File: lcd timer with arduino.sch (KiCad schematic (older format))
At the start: 30 parts, among them J1 Conn_01x05_Female, J2 Screw_Terminal_01x02, J3 Screw_Terminal_01x02, J4 Screw_Terminal_01x02, K1 SANYOU_SRD_Form_C, K2 SANYOU_SRD_Form_C, K3 SANYOU_SRD_Form_C, K4 SANYOU_SRD_Form_C, Q1 2N3904, Q2 2N3904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

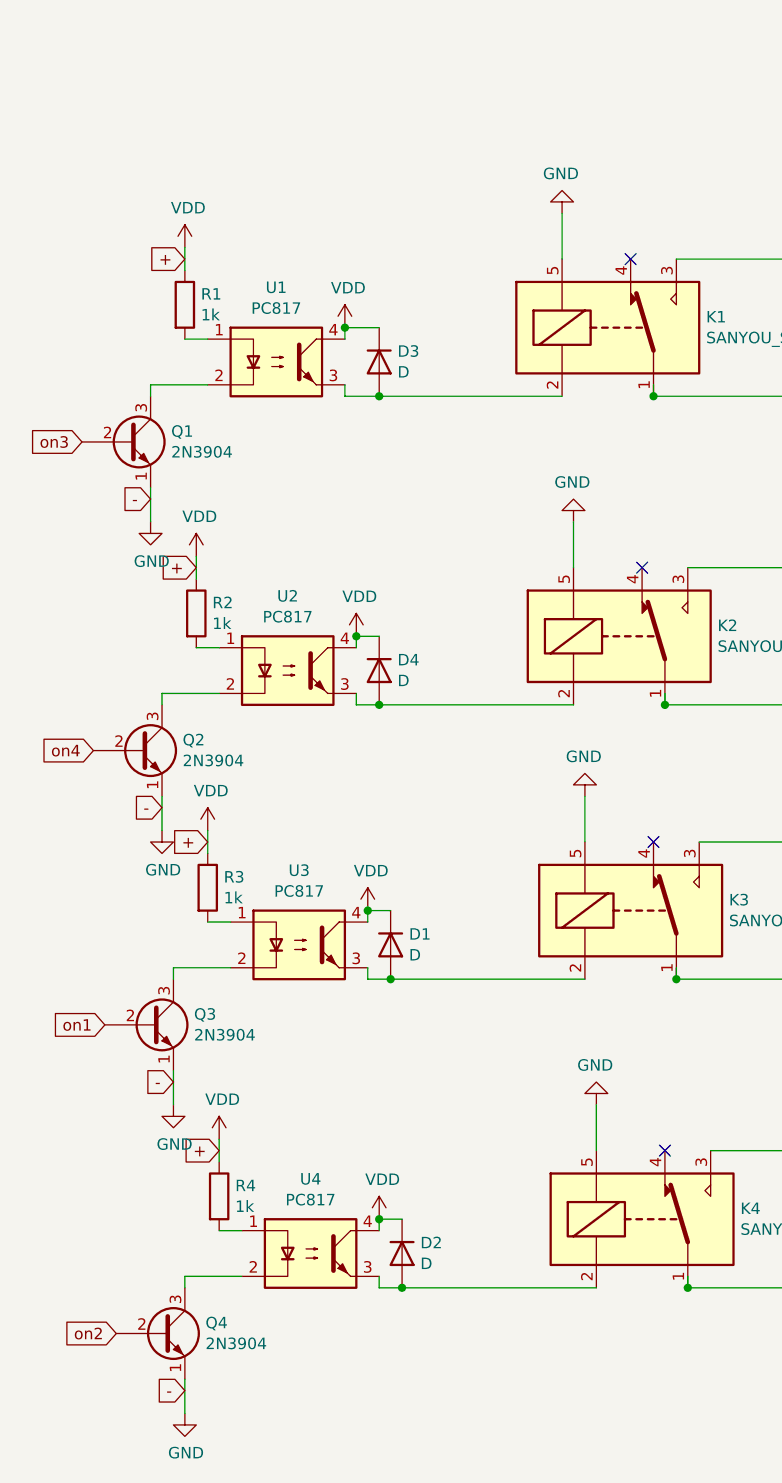
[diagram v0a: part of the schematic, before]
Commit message: fixed the schematic
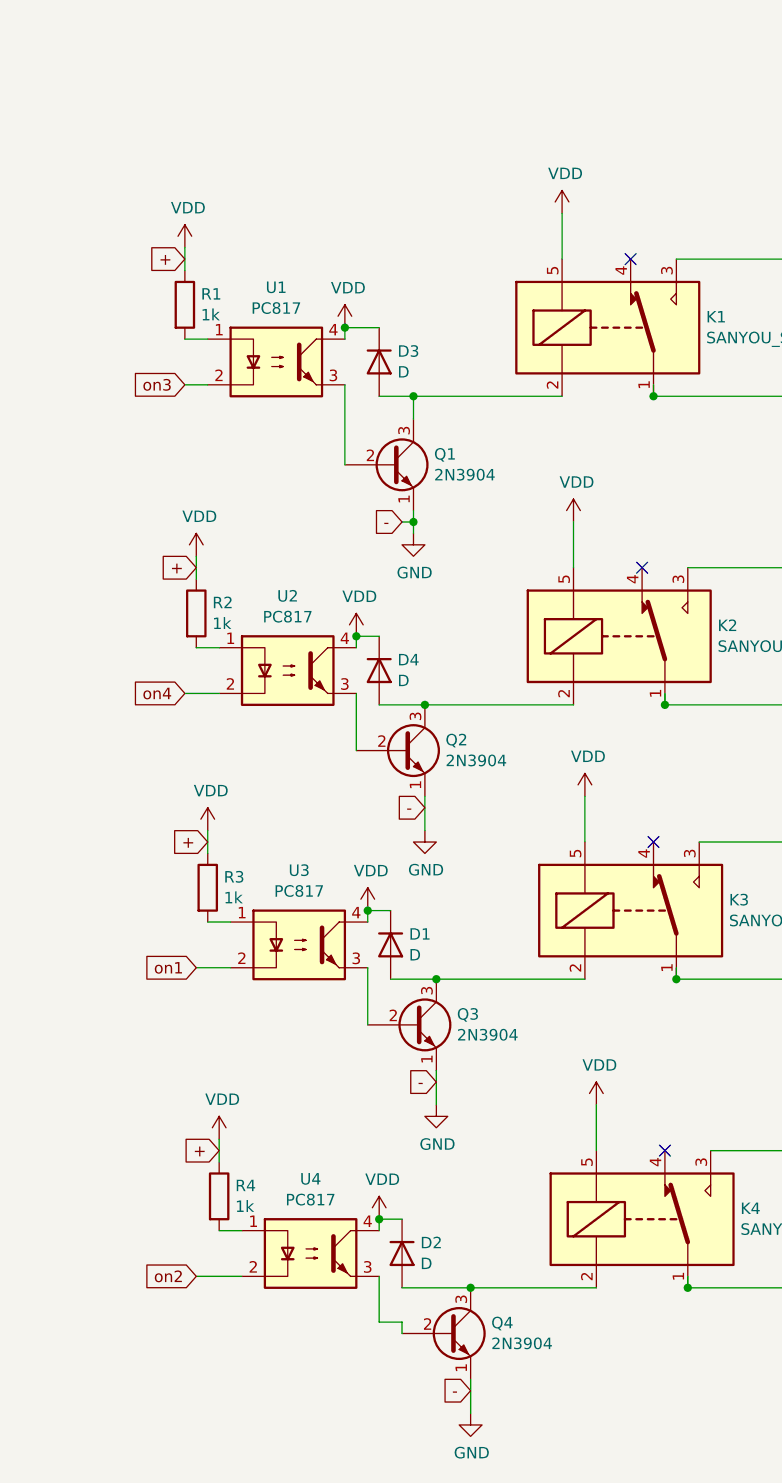
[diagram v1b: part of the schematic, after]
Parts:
- D1, D2, D3, D4: footprint Diode_THT:D_T-1_P5.08mm_Horizontal -> Diode_THT:D_T-1_P10.16mm_Horizontal
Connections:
- wire segments 85 -> 86
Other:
- moved on the sheet: Q1, Q2, Q3, Q4

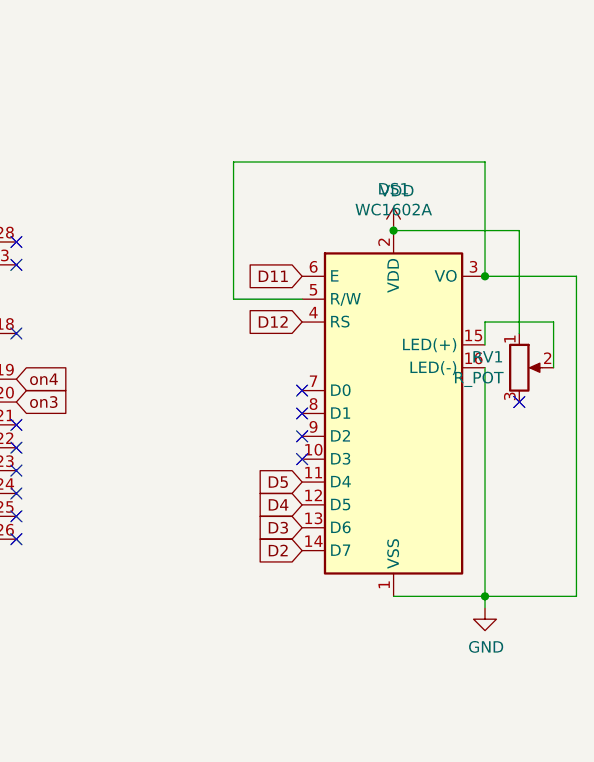
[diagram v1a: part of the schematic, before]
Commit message: fixed the schematic
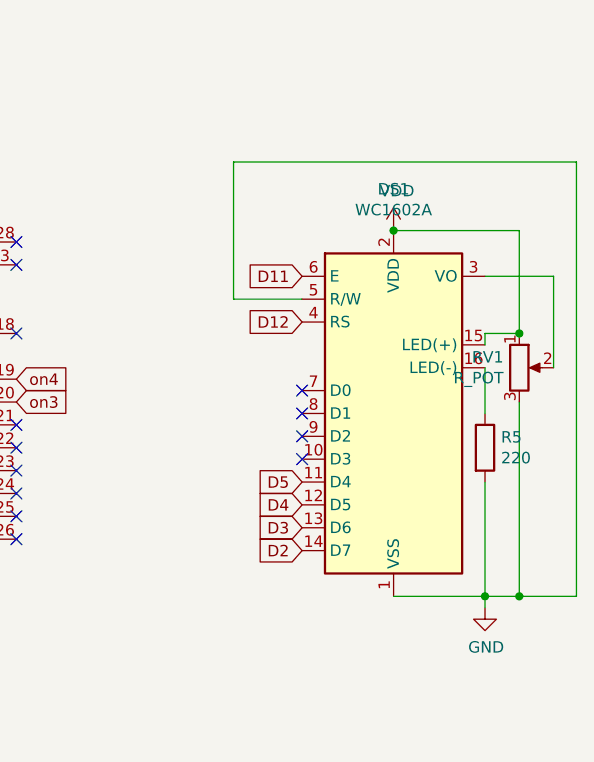
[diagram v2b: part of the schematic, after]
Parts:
- added R5: 220, Resistor_THT:R_Axial_DIN0309_L9.0mm_D3.2mm_P12.70mm_Horizontal, symbol Device:R
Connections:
- wire segments 86 -> 88
- no-connect marks 22 -> 21
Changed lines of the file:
@@
 D12
 Wire Wire Line
-	9500 4300 10600 4300
-Wire Wire Line
-	10600 4300 10600 4800
-Wire Wire Line
-	10600 4800 11000 4800
-Wire Wire Line
-	11000 4800 11000 6200
-Wire Wire Line
-	11000 6200 10600 6200
+	11000 6200 10750 6200
 $Comp
 L power:GND #PWR022
@@
 Wire Wire Line
 	10750 4600 10200 4600
-NoConn ~ 10750 5350
 $Comp
 L power:VDD #PWR019
@@
 $EndComp
 Connection ~ 10200 4600
-Connection ~ 10600 4800
 Wire Wire Line
 	9800 4900 9500 4900
@@
 $EndComp
 Wire Wire Line
-	10600 5100 10600 5000
-Wire Wire Line
-	10600 5000 10900 5000
-Wire Wire Line
-	10900 5000 10900 5200
-Wire Wire Line
-	10600 5200 10600 6200
+	10600 5200 10600 5400
 $Comp
 L Device:D D3
@@
 Wire Wire Line
 	1900 7100 2000 7100
+Wire Wire Line
+	10750 6200 10750 5350
+Connection ~ 10750 6200
+Wire Wire Line
+	10750 6200 10600 6200
+Wire Wire Line
+	9500 4300 11000 4300
+Wire Wire Line
+	11000 4300 11000 6200
+Wire Wire Line
+	10600 4800 10900 4800
+Wire Wire Line
+	10900 4800 10900 5200
+$Comp
+L Device:R R5
+U 1 1 604AD0CA
+P 10600 5550
+F 0 "R5" H 10670 5596 50  0000 L CNN
+F 1 "220" H 10670 5505 50  0000 L CNN
+F 2 "Resistor_THT:R_Axial_DIN0309_L9.0mm_D3.2mm_P12.70mm_Horizontal" V 10530 5550 50  0001 C CNN
+F 3 "~" H 10600 5550 50  0001 C CNN
+	1    10600 5550
+	1    0    0    -1
+$EndComp
+Wire Wire Line
+	10600 5100 10600 5050
+Wire Wire Line
+	10600 5050 10750 5050
+Connection ~ 10750 5050
+Wire Wire Line
+	10600 5700 10600 6200
 $EndSCHEMATC
